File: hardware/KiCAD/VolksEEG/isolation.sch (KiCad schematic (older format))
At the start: 0 parts

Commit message: Added Digi-key's kicad component libraries, some work done on power, think this will change but capturing it here for posterity.
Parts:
- added C?: 10u, Capacitor_SMD:C_0603_1608Metric_Pad1.08x0.95mm_HandSolder, symbol Device:C
- added C? (x2): 2.2u, Capacitor_SMD:C_0603_1608Metric_Pad1.08x0.95mm_HandSolder, symbol Device:C
- added L?: 3.3u, symbol Device:L
- added R?: R, symbol Device:R
- added U?: MEJ1S0305SC, MEJ1_SINGLE_SIP_MUR, symbol MEJ1S0305SC:MEJ1S0305SC
- added U? (x2): ADuM260N, Package_SO:SOIC-16W_7.5x12.8mm_P1.27mm, symbol Isolator:ADuM260N
- added U?: LP3990MF-3.3, VolksEEG:SOT95P280X145-5N, symbol VolksEEG:LP3990MF-3.3
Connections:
- net labels added: +3V3, +3V3_iso, ADS_nDRDY_iso, ADS_nDRDY_ni, GND2, GNDD, VDC
- net labels removed: ADS_DRDY_iso, ADS_DRDY_ni
- wire segments 0 -> 59
- no-connect marks 0 -> 1
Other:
- note added: "+3.3V@150mA"
- note added: "3.3V Digital Voltage Supply"

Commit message: Rejigged the power around so that the 3v3 supply is only generated once.
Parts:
- removed C?: 10u, Capacitor_SMD:C_0603_1608Metric_Pad1.08x0.95mm_HandSolder, symbol Device:C
- removed C? (x2): 2.2u, Capacitor_SMD:C_0603_1608Metric_Pad1.08x0.95mm_HandSolder, symbol Device:C
- removed L?: 3.3u, symbol Device:L
- removed R?: R, symbol Device:R
- removed U?: LP3990MF-3.3, VolksEEG:SOT95P280X145-5N, symbol VolksEEG:LP3990MF-3.3
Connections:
- net labels added: GNDA, VDD
- net labels removed: +3V3, GND2
- wire segments 59 -> 39
- no-connect marks 1 -> 0
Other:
- note removed: "+3.3V@150mA"
- note removed: "3.3V Digital Voltage Supply"
- moved on the sheet: U?

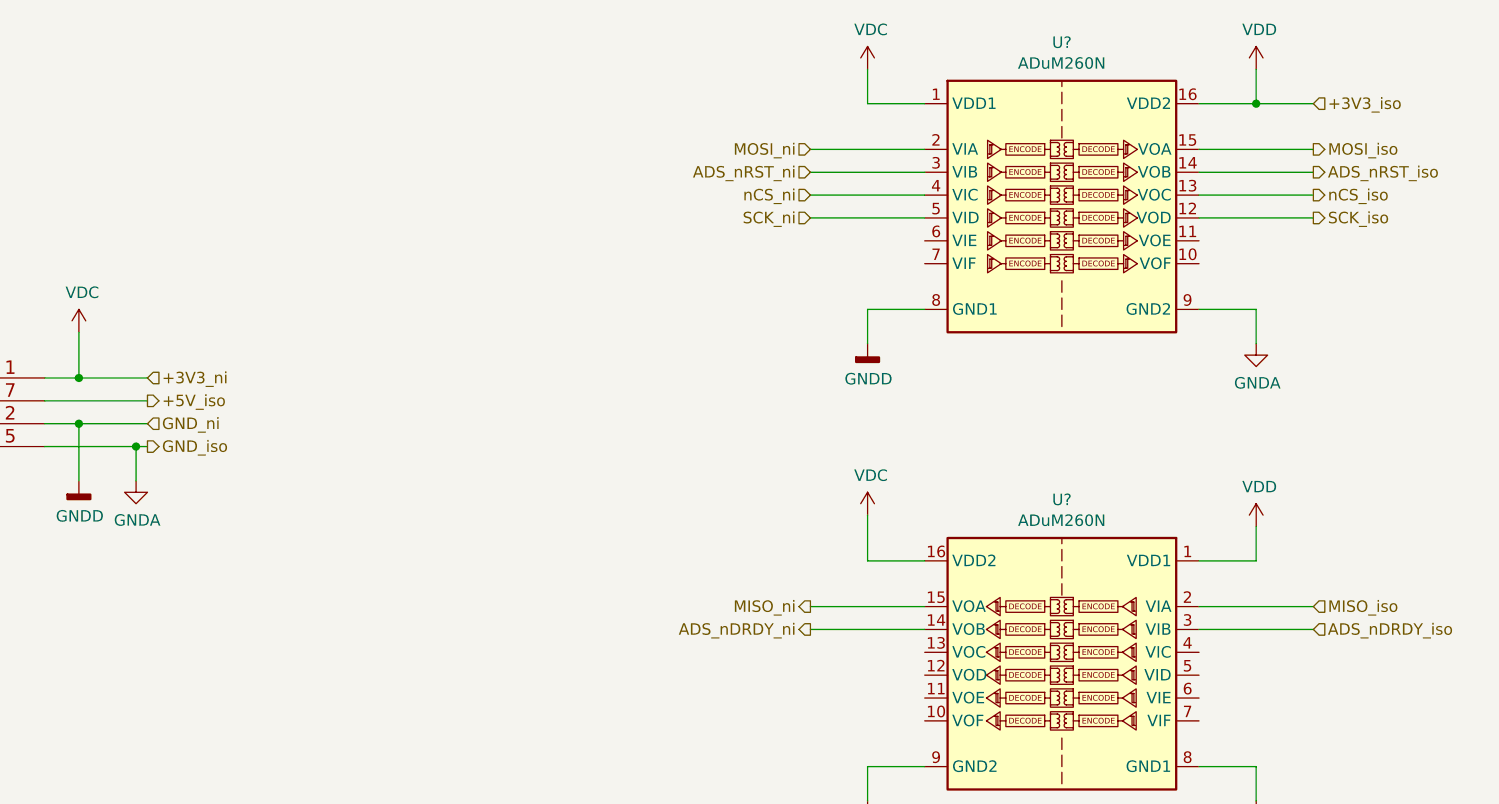
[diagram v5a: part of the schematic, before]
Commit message: Updated names of heirarchical pins, finished referential montage configuration, added filter cap to ADS_nRST line, started putting ADS1299 gpios to a header.
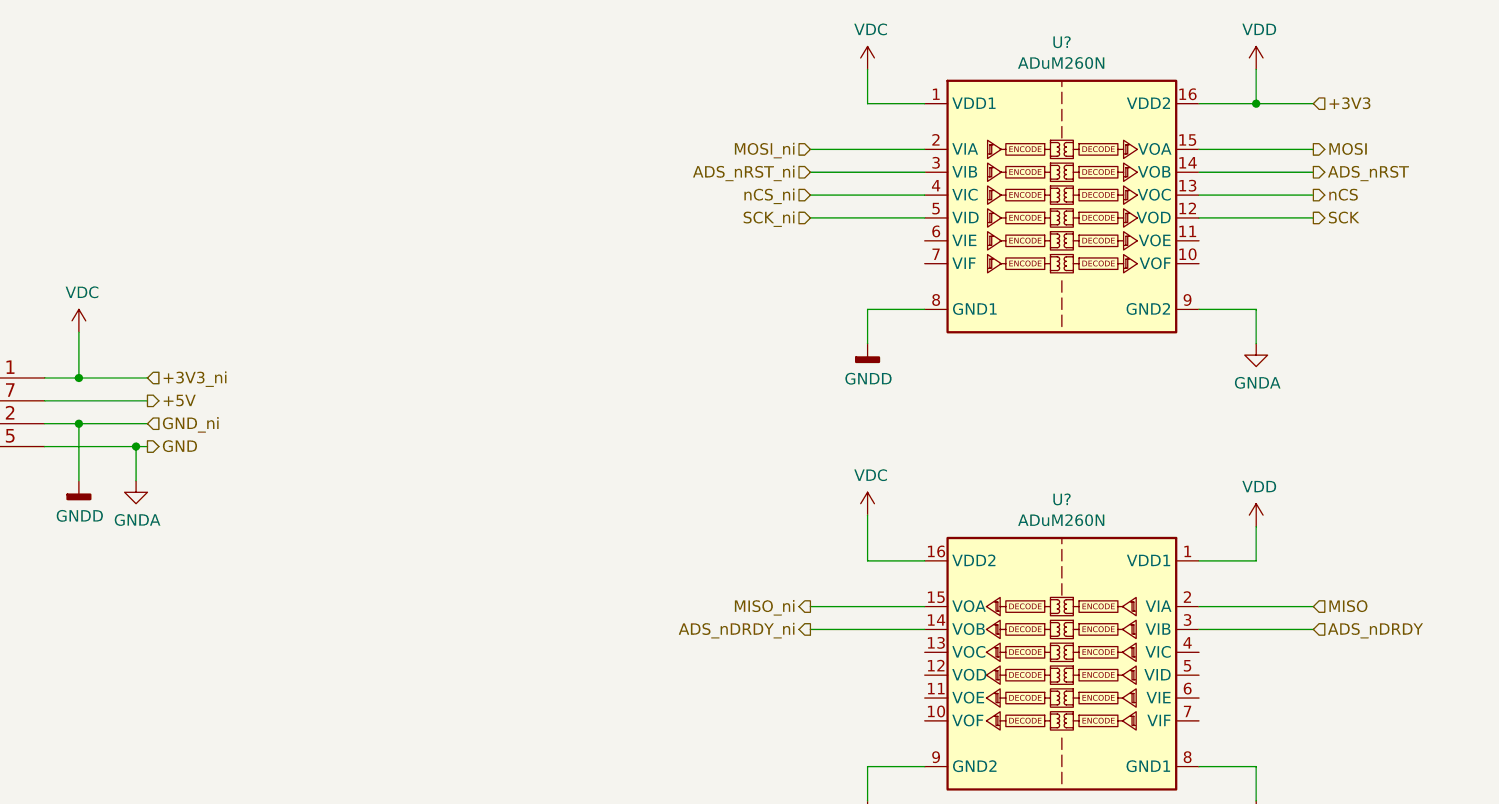
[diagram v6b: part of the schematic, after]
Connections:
- net +5V_iso renamed +5V
- net ADS_nDRDY_iso renamed ADS_nDRDY
- net ADS_nRST_iso renamed ADS_nRST
- net MISO_iso renamed MISO
- net MOSI_iso renamed MOSI
- net SCK_iso renamed SCK
- net nCS_iso renamed nCS
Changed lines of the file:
@@
 GND_ni
 Text HLabel 8800 2550 2    50   Output ~ 0
-MOSI_iso
+MOSI
 Text HLabel 8800 2650 2    50   Output ~ 0
-ADS_nRST_iso
+ADS_nRST
 Text HLabel 8800 2750 2    50   Output ~ 0
-nCS_iso
+nCS
 Text HLabel 8800 2850 2    50   Output ~ 0
-SCK_iso
+SCK
 Text HLabel 8800 4550 2    50   Input ~ 0
-MISO_iso
+MISO
 Text HLabel 8800 4650 2    50   Input ~ 0
-ADS_nDRDY_iso
+ADS_nDRDY
 Text HLabel 3700 3850 2    50   Output ~ 0
-GND_iso
+GND
 $Comp
 L MEJ1S0305SC:MEJ1S0305SC U?
@@
 	7100 4650 6600 4650
 Text HLabel 3700 3650 2    50   Output ~ 0
-+5V_iso
++5V
 Wire Wire Line
 	3250 3650 3700 3650
@@
 $EndComp
 Text HLabel 8800 2350 2    50   Input ~ 0
-+3V3_iso
++3V3
 Wire Wire Line
 	8800 2350 8550 2350

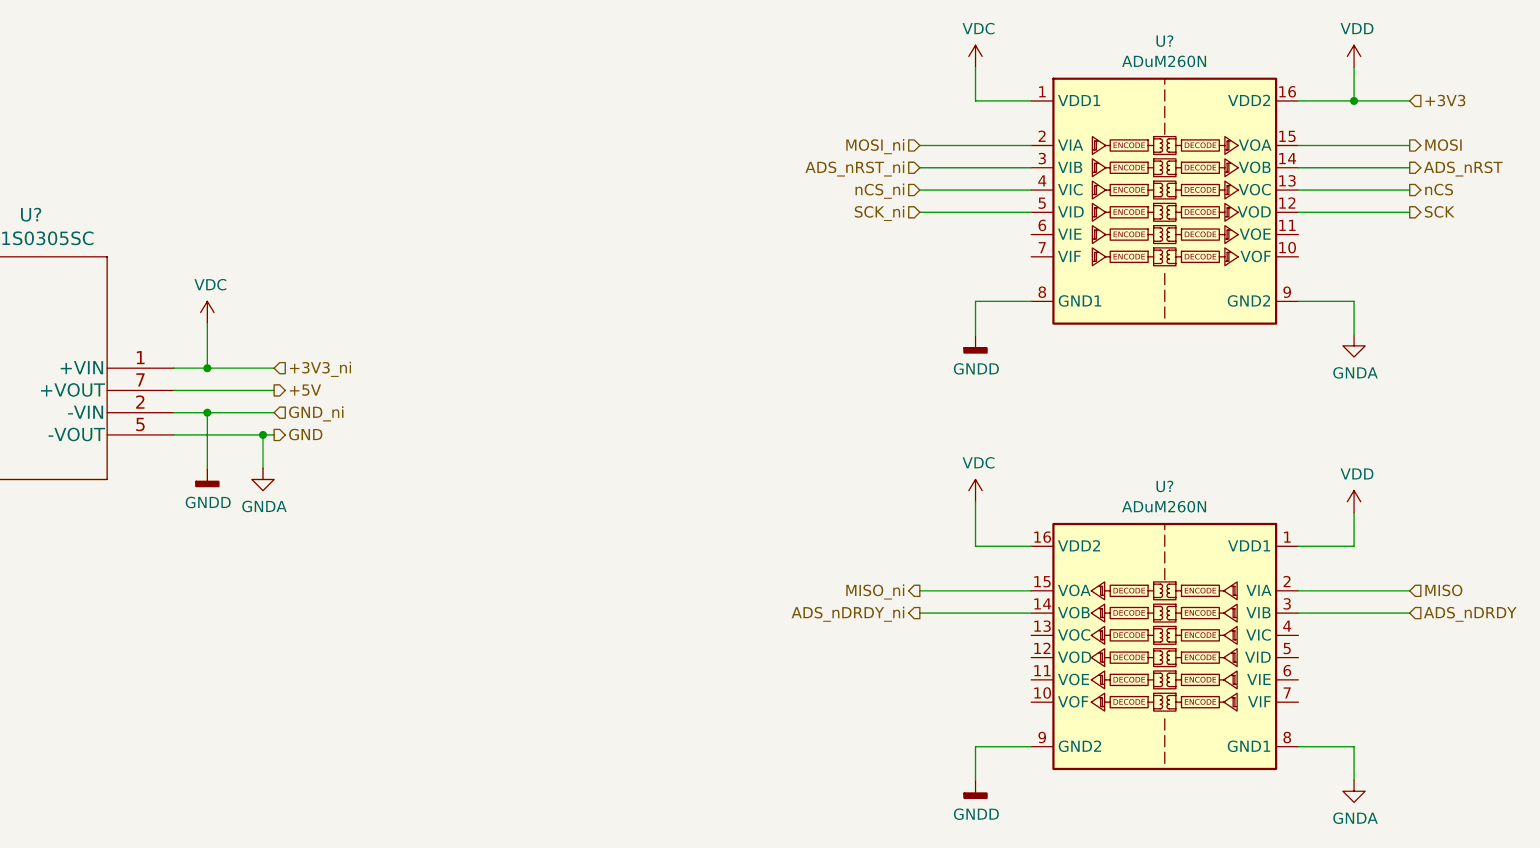
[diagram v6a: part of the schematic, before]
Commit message: Added custom power symbols for non isolated power. Seperated Analogue and digital supplies. finished putting the ADS1299 GPIOs to a header.
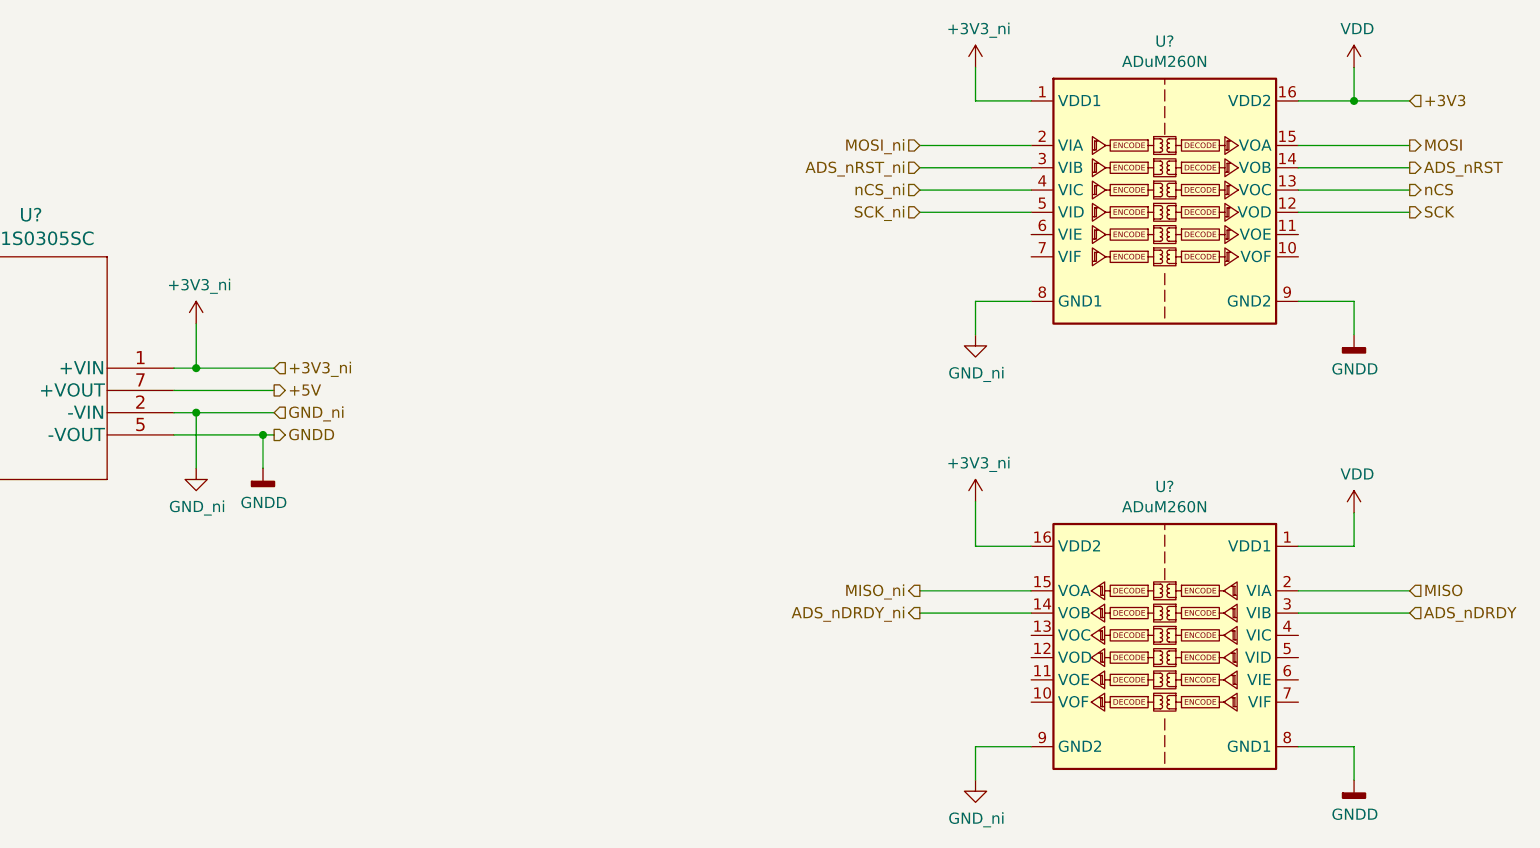
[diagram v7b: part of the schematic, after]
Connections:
- net GNDA is gone; now on net GNDD: U?.5 (-VOUT), U?.8 (GND1), U?.9 (GND2)
- net VDD is gone; now on net +3V3: U?.1 (VDD1), U?.16 (VDD2)
- net GNDD: no longer U?.2 (-VIN), U?.8 (GND1), U?.9 (GND2)
- net VDC renamed +3V3
- new net GND: U?.2 (-VIN), U?.8 (GND1), U?.9 (GND2)
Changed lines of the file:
@@
 ADS_nDRDY
 Text HLabel 3700 3850 2    50   Output ~ 0
-GND
+GNDD
 $Comp
 L MEJ1S0305SC:MEJ1S0305SC U?
@@
 $EndComp
 Wire Wire Line
-	3250 3550 3400 3550
-Wire Wire Line
-	3250 3750 3400 3750
+	3250 3550 3350 3550
+Wire Wire Line
+	3250 3750 3350 3750
 Wire Wire Line
 	3700 3850 3650 3850
@@
 $EndComp
 Wire Wire Line
-	3400 3350 3400 3550
-Connection ~ 3400 3550
-Wire Wire Line
-	3400 3550 3700 3550
-Wire Wire Line
-	3400 4000 3400 3750
-Connection ~ 3400 3750
-Wire Wire Line
-	3400 3750 3700 3750
+	3350 3350 3350 3550
+Connection ~ 3350 3550
+Wire Wire Line
+	3350 3550 3700 3550
+Wire Wire Line
+	3350 4000 3350 3750
+Connection ~ 3350 3750
+Wire Wire Line
+	3350 3750 3700 3750
 Wire Wire Line
 	3650 4000 3650 3850
@@
 	8550 5250 8300 5250
 $Comp
-L power:VDC #PWR?
-U 1 1 618DEE6D
-P 3400 3350
-F 0 "#PWR?" H 3400 3250 50  0001 C CNN
-F 1 "VDC" H 3415 3523 50  0000 C CNN
-F 2 "" H 3400 3350 50  0001 C CNN
-F 3 "" H 3400 3350 50  0001 C CNN
-	1    3400 3350
-	1    0    0    -1
-$EndComp
-$Comp
-L power:VDC #PWR?
-U 1 1 618DF1EE
-P 6850 2200
-F 0 "#PWR?" H 6850 2100 50  0001 C CNN
-F 1 "VDC" H 6865 2373 50  0000 C CNN
-F 2 "" H 6850 2200 50  0001 C CNN
-F 3 "" H 6850 2200 50  0001 C CNN
-	1    6850 2200
-	1    0    0    -1
-$EndComp
-$Comp
-L power:VDC #PWR?
-U 1 1 618DF626
-P 6850 4150
-F 0 "#PWR?" H 6850 4050 50  0001 C CNN
-F 1 "VDC" H 6865 4323 50  0000 C CNN
-F 2 "" H 6850 4150 50  0001 C CNN
-F 3 "" H 6850 4150 50  0001 C CNN
-	1    6850 4150
-	1    0    0    -1
-$EndComp
-$Comp
-L power:GNDD #PWR?
-U 1 1 618E15C2
-P 3400 4000
-AR Path="/615BA20B/618E15C2" Ref="#PWR?"  Part="1"
-AR Path="/61731DC5/618E15C2" Ref="#PWR?"  Part="1"
-F 0 "#PWR?" H 3400 3750 50  0001 C CNN
-F 1 "GNDD" H 3404 3845 50  0000 C CNN
-F 2 "" H 3400 4000 50  0001 C CNN
-F 3 "" H 3400 4000 50  0001 C CNN
-	1    3400 4000
-	1    0    0    -1
-$EndComp
-$Comp
 L power:GNDD #PWR?
 U 1 1 618E335E
-P 6850 3400
+P 8550 3400
 AR Path="/615BA20B/618E335E" Ref="#PWR?"  Part="1"
 AR Path="/61731DC5/618E335E" Ref="#PWR?"  Part="1"
-F 0 "#PWR?" H 6850 3150 50  0001 C CNN
-F 1 "GNDD" H 6854 3245 50  0000 C CNN
-F 2 "" H 6850 3400 50  0001 C CNN
-F 3 "" H 6850 3400 50  0001 C CNN
-	1    6850 3400
+F 0 "#PWR?" H 8550 3150 50  0001 C CNN
+F 1 "GNDD" H 8554 3245 50  0000 C CNN
+F 2 "" H 8550 3400 50  0001 C CNN
+F 3 "" H 8550 3400 50  0001 C CNN
+	1    8550 3400
 	1    0    0    -1
 $EndComp
@@
 L power:GNDD #PWR?
 U 1 1 618E3648
-P 6850 5400
+P 8550 5400
 AR Path="/615BA20B/618E3648" Ref="#PWR?"  Part="1"
 AR Path="/61731DC5/618E3648" Ref="#PWR?"  Part="1"
-F 0 "#PWR?" H 6850 5150 50  0001 C CNN
-F 1 "GNDD" H 6854 5245 50  0000 C CNN
-F 2 "" H 6850 5400 50  0001 C CNN
-F 3 "" H 6850 5400 50  0001 C CNN
-	1    6850 5400
+F 0 "#PWR?" H 8550 5150 50  0001 C CNN
+F 1 "GNDD" H 8554 5245 50  0000 C CNN
+F 2 "" H 8550 5400 50  0001 C CNN
+F 3 "" H 8550 5400 50  0001 C CNN
+	1    8550 5400
 	1    0    0    -1
 $EndComp
@@
 $EndComp
 $Comp
-L power:GNDA #PWR?
-U 1 1 61A689C8
-P 8550 5400
-AR Path="/615BA255/61A689C8" Ref="#PWR?"  Part="1"
-AR Path="/61731DC5/61A689C8" Ref="#PWR?"  Part="1"
-F 0 "#PWR?" H 8550 5150 50  0001 C CNN
-F 1 "GNDA" H 8555 5227 50  0000 C CNN
-F 2 "" H 8550 5400 50  0001 C CNN
-F 3 "" H 8550 5400 50  0001 C CNN
-	1    8550 5400
-	1    0    0    -1
-$EndComp
-$Comp
-L power:GNDA #PWR?
-U 1 1 61A6924F
-P 8550 3400
-AR Path="/615BA255/61A6924F" Ref="#PWR?"  Part="1"
-AR Path="/61731DC5/61A6924F" Ref="#PWR?"  Part="1"
-F 0 "#PWR?" H 8550 3150 50  0001 C CNN
-F 1 "GNDA" H 8555 3227 50  0000 C CNN
-F 2 "" H 8550 3400 50  0001 C CNN
-F 3 "" H 8550 3400 50  0001 C CNN
-	1    8550 3400
-	1    0    0    -1
-$EndComp
-$Comp
-L power:GNDA #PWR?
-U 1 1 61A69B30
+L VolksEEG:+3V3_ni #PWR?
+U 1 1 61BD5B0A
+P 3350 3350
+F 0 "#PWR?" H 3350 3200 50  0001 C CNN
+F 1 "+3V3_ni" H 3365 3523 50  0000 C CNN
+F 2 "" H 3350 3350 50  0001 C CNN
+F 3 "" H 3350 3350 50  0001 C CNN
+	1    3350 3350
+	1    0    0    -1
+$EndComp
+$Comp
+L VolksEEG:GND_ni #PWR?
+U 1 1 61BD6486
+P 3350 4000
+F 0 "#PWR?" H 3350 3750 50  0001 C CNN
+F 1 "GND_ni" H 3355 3827 50  0000 C CNN
+F 2 "" H 3350 4000 50  0001 C CNN
+F 3 "" H 3350 4000 50  0001 C CNN
+	1    3350 4000
+	1    0    0    -1
+$EndComp
+$Comp
+L power:GNDD #PWR?
+U 1 1 61BD6D15
 P 3650 4000
-AR Path="/615BA255/61A69B30" Ref="#PWR?"  Part="1"
-AR Path="/61731DC5/61A69B30" Ref="#PWR?"  Part="1"
 F 0 "#PWR?" H 3650 3750 50  0001 C CNN
-F 1 "GNDA" H 3655 3827 50  0000 C CNN
+F 1 "GNDD" H 3654 3845 50  0000 C CNN
 F 2 "" H 3650 4000 50  0001 C CNN
 F 3 "" H 3650 4000 50  0001 C CNN
@@
 	1    0    0    -1
 $EndComp
+$Comp
+L VolksEEG:GND_ni #PWR?
+U 1 1 61BD8AA1
+P 6850 3400
+F 0 "#PWR?" H 6850 3150 50  0001 C CNN
+F 1 "GND_ni" H 6855 3227 50  0000 C CNN
+F 2 "" H 6850 3400 50  0001 C CNN
+F 3 "" H 6850 3400 50  0001 C CNN
+	1    6850 3400
+	1    0    0    -1
+$EndComp
+$Comp
+L VolksEEG:GND_ni #PWR?
+U 1 1 61BD8EDB
+P 6850 5400
+F 0 "#PWR?" H 6850 5150 50  0001 C CNN
+F 1 "GND_ni" H 6855 5227 50  0000 C CNN
+F 2 "" H 6850 5400 50  0001 C CNN
+F 3 "" H 6850 5400 50  0001 C CNN
+	1    6850 5400
+	1    0    0    -1
+$EndComp
+$Comp
+L VolksEEG:+3V3_ni #PWR?
+U 1 1 61BD925C
+P 6850 2200
+F 0 "#PWR?" H 6850 2050 50  0001 C CNN
+F 1 "+3V3_ni" H 6865 2373 50  0000 C CNN
+F 2 "" H 6850 2200 50  0001 C CNN
+F 3 "" H 6850 2200 50  0001 C CNN
+	1    6850 2200
+	1    0    0    -1
+$EndComp
+$Comp
+L VolksEEG:+3V3_ni #PWR?
+U 1 1 61BD96F3
+P 6850 4150
+F 0 "#PWR?" H 6850 4000 50  0001 C CNN
+F 1 "+3V3_ni" H 6865 4323 50  0000 C CNN
+F 2 "" H 6850 4150 50  0001 C CNN
+F 3 "" H 6850 4150 50  0001 C CNN
+	1    6850 4150
+	1    0    0    -1
+$EndComp
